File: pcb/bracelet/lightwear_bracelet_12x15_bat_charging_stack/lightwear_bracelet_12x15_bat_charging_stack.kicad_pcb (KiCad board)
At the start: 2 copper layers, 2.8 x 7.8 mm, 6 parts

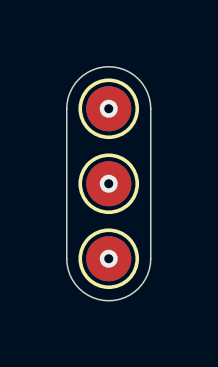
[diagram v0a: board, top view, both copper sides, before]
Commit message: fix footprint for sot-883 mosfet, add pads for flex button board
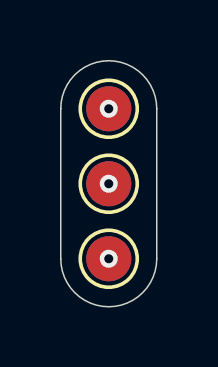
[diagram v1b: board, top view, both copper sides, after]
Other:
- board size 2.8 x 7.8 mm -> 3.2 x 8.2 mm
- copper layers 2 -> 6
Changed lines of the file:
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@@
 	(layers
 		(0 "F.Cu" signal)
+		(4 "In1.Cu" signal)
+		(6 "In2.Cu" signal)
+		(8 "In3.Cu" signal)
+		(10 "In4.Cu" signal)
 		(2 "B.Cu" signal)
 		(9 "F.Adhes" user "F.Adhesive")
@@
 	)
 	(setup
+		(stackup
+			(layer "F.SilkS"
+				(type "Top Silk Screen")
+			)
+			(layer "F.Paste"
+				(type "Top Solder Paste")
+			)
+			(layer "F.Mask"
+				(type "Top Solder Mask")
+				(thickness 0.01)
+			)
+			(layer "F.Cu"
+				(type "copper")
+				(thickness 0.035)
+			)
+			(layer "dielectric 1"
+				(type "prepreg")
+				(thickness 0.1)
+				(material "FR4")
+				(epsilon_r 4.5)
+				(loss_tangent 0.02)
+			)
+			(layer "In1.Cu"
+				(type "copper")
+				(thickness 0.035)
+			)
+			(layer "dielectric 2"
+				(type "core")
+				(thickness 0.535)
+				(material "FR4")
+				(epsilon_r 4.5)
+				(loss_tangent 0.02)
+			)
+			(layer "In2.Cu"
+				(type "copper")
+				(thickness 0.035)
+			)
+			(layer "dielectric 3"
+				(type "prepreg")
+				(thickness 0.1)
+				(material "FR4")
+				(epsilon_r 4.5)
+				(loss_tangent 0.02)
+			)
+			(layer "In3.Cu"
+				(type "copper")
+				(thickness 0.035)
+			)
+			(layer "dielectric 4"
+				(type "core")
+				(thickness 0.535)
+				(material "FR4")
+				(epsilon_r 4.5)
+				(loss_tangent 0.02)
+			)
+			(layer "In4.Cu"
+				(type "copper")
+				(thickness 0.035)
+			)
+			(layer "dielectric 5"
+				(type "prepreg")
+				(thickness 0.1)
+				(material "FR4")
+				(epsilon_r 4.5)
+				(loss_tangent 0.02)
+			)
+			(layer "B.Cu"
+				(type "copper")
+				(thickness 0.035)
+			)
+			(layer "B.Mask"
+				(type "Bottom Solder Mask")
+				(thickness 0.01)
+			)
+			(layer "B.Paste"
+				(type "Bottom Solder Paste")
+			)
+			(layer "B.SilkS"
+				(type "Bottom Silk Screen")
+			)
+			(copper_finish "None")
+			(dielectric_constraints no)
+		)
 		(pad_to_mask_clearance 0)
 		(allow_soldermask_bridges_in_footprints no)
@@
 			(outputformat 1)
 			(mirror no)
-			(drillshape 1)
+			(drillshape 0)
 			(scaleselection 1)
-			(outputdirectory "")
+			(outputdirectory "rev0")
 		)
 	)
@@
 	)
 	(gr_arc
-		(start 151.4 108)
-		(mid 150 109.4)
-		(end 148.6 108)
+		(start 151.6 108)
+		(mid 150 109.6)
+		(end 148.4 108)
 		(stroke
 			(width 0.05)
@@
 	)
 	(gr_line
-		(start 151.4 103)
-		(end 151.4 108)
+		(start 151.6 103)
+		(end 151.6 108)
 		(stroke
 			(width 0.05)
@@
 	)
 	(gr_arc
-		(start 148.6 103)
-		(mid 150 101.6)
-		(end 151.4 103)
+		(start 148.4 103)
+		(mid 150 101.4)
+		(end 151.6 103)
 		(stroke
 			(width 0.05)
@@
 	)
 	(gr_line
-		(start 148.6 103)
-		(end 148.6 108)
+		(start 148.4 103)
+		(end 148.4 108)
 		(stroke
 			(width 0.05)
